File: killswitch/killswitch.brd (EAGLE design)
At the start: 30.5 x 30.5 mm, 22 parts

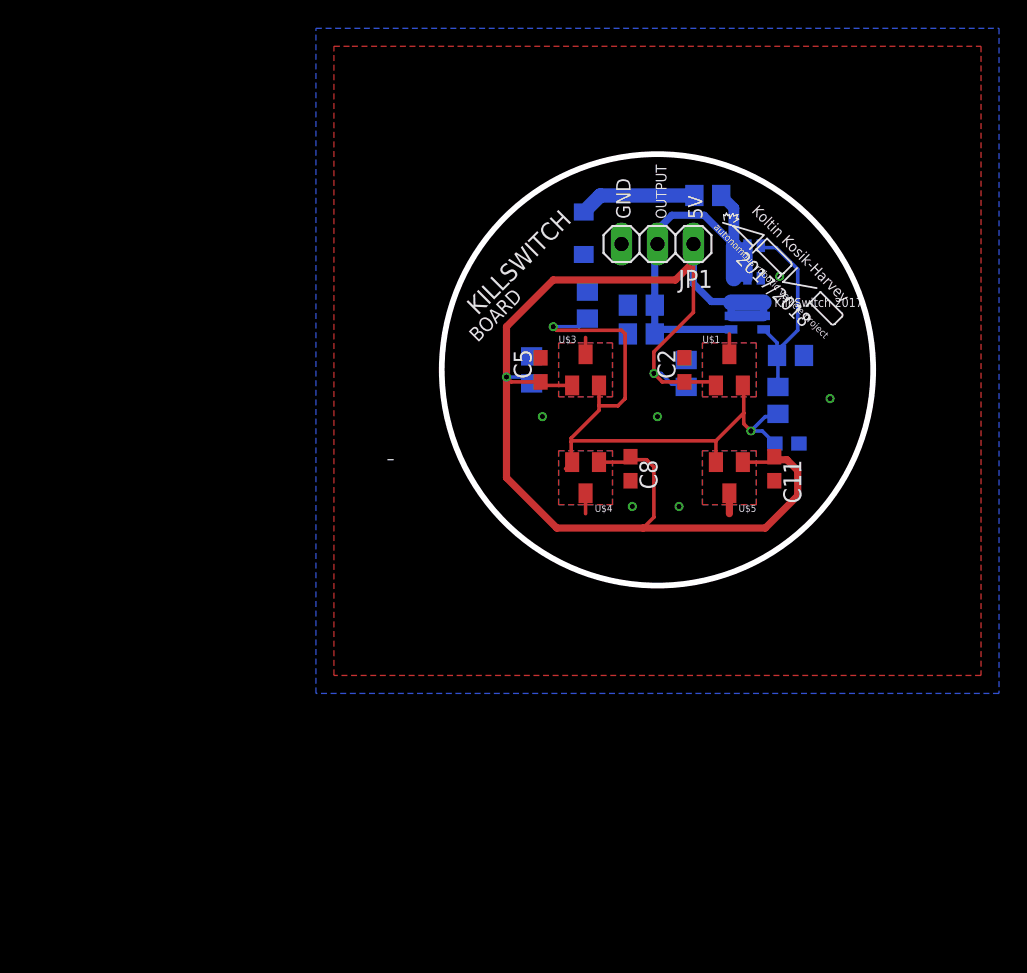
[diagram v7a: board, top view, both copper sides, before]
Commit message: Centered Hall Sensors, added surface mount header
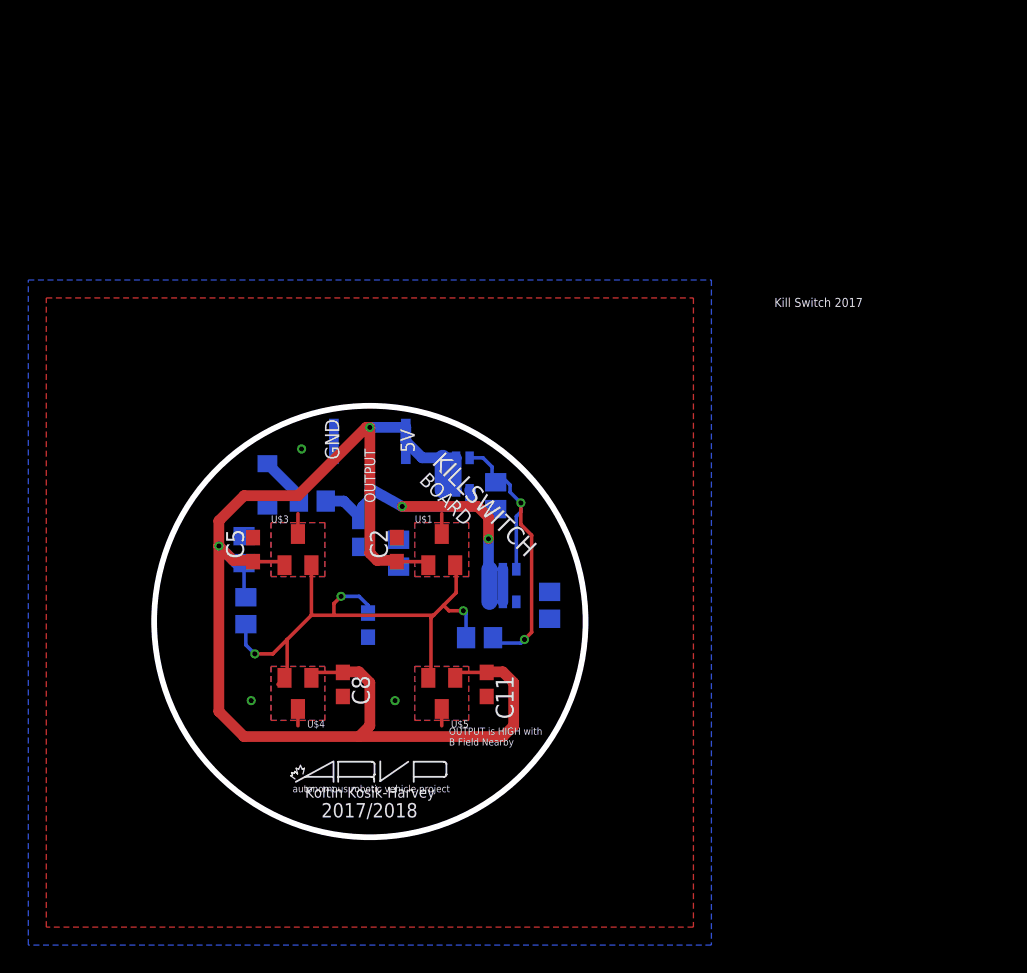
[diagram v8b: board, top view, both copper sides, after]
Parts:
- JP1: value (none) -> 1241150-3; device pinhead:1X03 -> KillSwitch:CONN_1241150-3_TYCO
- moved U$2 49.7 mm to (-5.46, -12.1), turned to 0 degrees
- moved R4 35.3 mm to (-4.06, 8.51)
- moved R6 32.4 mm to (-8.76, 0.76)
- moved C3 32.3 mm to (-0.13, -0.25), turned to 270 degrees
- moved U$8 28.7 mm to (9.40, 2.54)
- moved LED1 28.6 mm to (-7.24, 9.65)
- moved R9 26.9 mm to (7.75, -1.14), turned to 180 degrees
- moved C11 25.4 mm to (8.26, -4.45)
- moved C8 25.4 mm to (-1.91, -4.45)
- moved JP1 25.4 mm to (0.00, 11.4), flipped to the bottom, turned to 0 degrees
- moved U$4 25.4 mm to (-5.08, -5.08)
- moved U$5 25.4 mm to (5.08, -5.08)
- moved C13 24.2 mm to (-0.51, 6.22), turned to 270 degrees
- moved C1 24.0 mm to (2.03, 4.83)
- moved C2 24.0 mm to (1.91, 5.08)
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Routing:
- net N$10: track 14.5 -> 23.3 mm, vias 0 -> 2
- net N$8: track 8.30 -> 3.56 mm
- net N$5: track 43.9 -> 39.7 mm, vias 2 -> 3
- net OUTPUT: track 30.4 -> 31.6 mm, vias 0 -> 2
- net +5V: track 102.5 -> 101.6 mm
- net GND: track 5.51 -> 5.25 mm, vias 6 -> 3
